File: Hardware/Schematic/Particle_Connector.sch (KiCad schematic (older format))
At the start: 10 parts, among them J1 Conn_01x12, J2 Conn_01x12, J6 Conn_01x12, J7 Conn_01x12

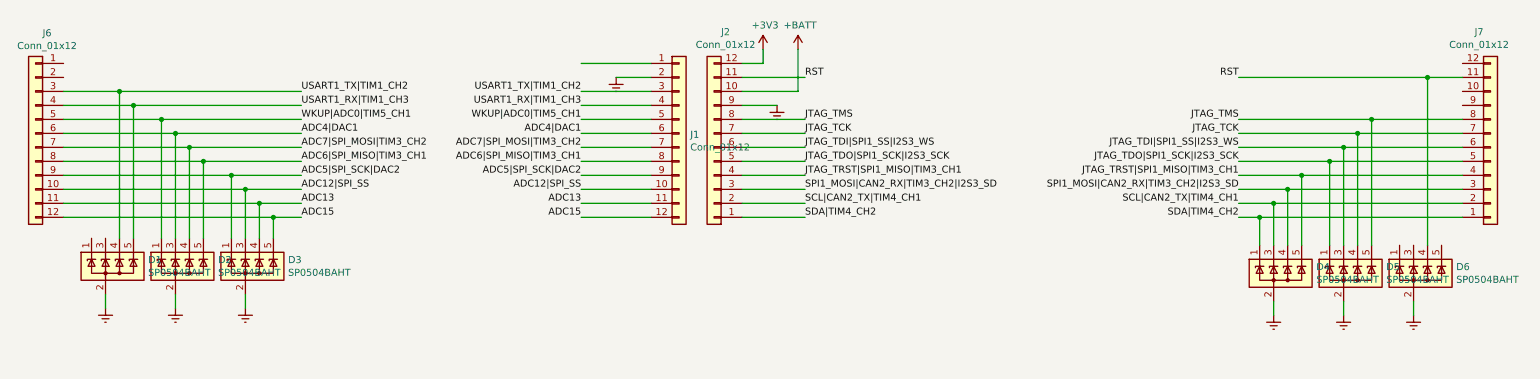
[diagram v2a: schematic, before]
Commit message: Lots of schematic updates
Lots of stuff...

* Added a new 8-pin TVS diode array
* Finalized the display connector
* Corrected the net labels to global labels so they span across sheets
* Added a 5V linear voltage regulator and LEDs to debug power
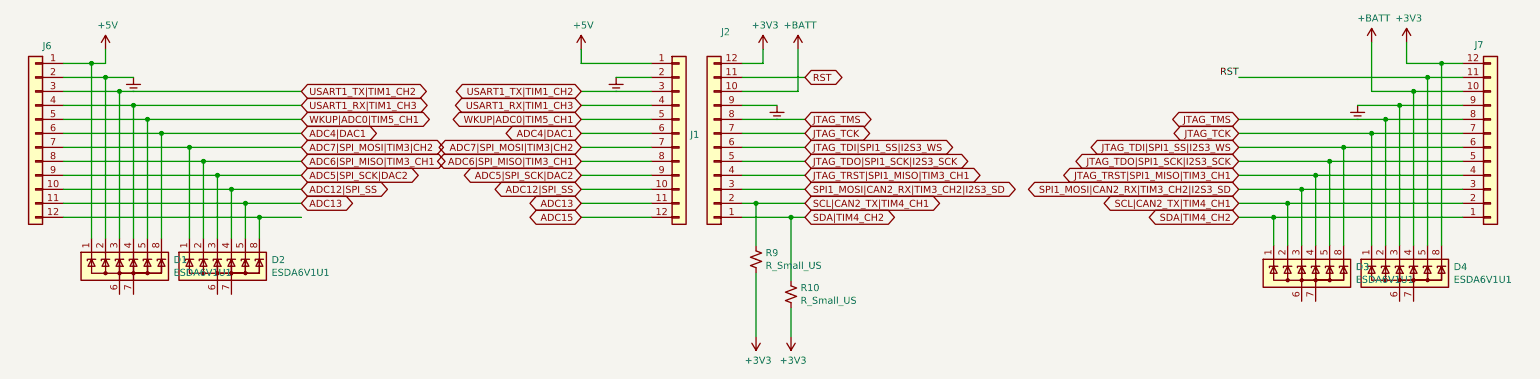
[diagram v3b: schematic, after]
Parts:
- removed D1, D2, D3, D4, D5, D6: SP0504BAHT, Package_TO_SOT_SMD:SOT-23-5, symbol Power_Protection:SP0504BAHT
- added D1, D2, D3, D4: ESDA6V1U1, ESDA6V1U1:SOIC127P600X175-8N, symbol Power_Protection:ESDA6V1U1
- added R10, R9: R_Small_US, Resistor_SMD:R_2512_6332Metric_Pad1.52x3.35mm_HandSolder, symbol Device:R_Small_US
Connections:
- net +3V3: now also J7.12 (Pin_12), D4.8 (K), R10.2, R9.2
- net +BATT: now also J7.10 (Pin_10), D4.4 (K)
- net ADC12|SPI_SS: now also D2.4 (K)
- net ADC13: now also D2.5 (K)
- net ADC15: no longer J6.12 (Pin_12)
- net ADC4|DAC1: now also D1.8 (K)
- net ADC5|SPI_SCK|DAC2: now also D2.3 (K)
- net ADC6|SPI_MISO|TIM3_CH1: now also D2.2 (K)
- net Earth: now also J6.2 (Pin_2), J7.9 (Pin_9), D1.2 (K), D4.3 (K)
- net JTAG_TCK: now also D4.1 (K)
- net JTAG_TDI|SPI1_SS|I2S3_WS: now also D3.8 (K)
- net JTAG_TDO|SPI1_SCK|I2S3_SCK: now also D3.5 (K)
- net JTAG_TMS: now also D4.2 (K)
- net JTAG_TRST|SPI1_MISO|TIM3_CH1: now also D3.4 (K)
- net RST: now also D4.5 (K)
- net SCL|CAN2_TX|TIM4_CH1: now also D3.2 (K), R9.1
- net SDA|TIM4_CH2: now also D3.1 (K), R10.1
- net SPI1_MOSI|CAN2_RX|TIM3_CH2|I2S3_SD: now also D3.3 (K)
- net USART1_RX|TIM1_CH3: now also D1.4 (K)
- net USART1_TX|TIM1_CH2: now also D1.3 (K)
- net WKUP|ADC0|TIM5_CH1: now also D1.5 (K)
- net +5V: now reaches J1.1 (Pin_1)
- net +5V: now also J6.1 (Pin_1), D1.1 (K)
- net ADC7|SPI_MOSI|TIM3_CH2 renamed ADC7|SPI_MOSI|TIM3|CH2
- net ADC7|SPI_MOSI|TIM3|CH2: now also D2.1 (K)
- new net: D2.8 (K), J6.12 (Pin_12)

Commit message: Added pogo-pin test points for "Extra" photon lines. Also added a 32-pin vertical header for connecting multiple smaller boards.
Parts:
- added J11, J12, J14, J15, J16, J17, J18: Conn_01x01, TestPoint:TestPoint_THTPad_1.0x1.0mm_Drill0.5mm, symbol Connector_Generic:Conn_01x01
- added J?: Conn_01x32, Connector_PinHeader_1.00mm:PinHeader_1x32_P1.00mm_Horizontal, symbol Connector_Generic:Conn_01x32
- D1, D2, D3, D4: symbol Power_Protection:ESDA6V1U1 -> WiFiLMR-rescue:ESDA6V1U1-Power_Protection
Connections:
- net +3V3: now also J?.24 (Pin_24)
- net +5V: now also J?.1 (Pin_1)
- net +BATT: now also J?.22 (Pin_22)
- net ADC12|SPI_SS: now also J?.10 (Pin_10)
- net ADC13: now also J?.11 (Pin_11)
- net ADC15: now also J?.12 (Pin_12)
- net ADC4|DAC1: now also J?.6 (Pin_6)
- net ADC5|SPI_SCK|DAC2: now also J?.9 (Pin_9)
- net ADC6|SPI_MISO|TIM3_CH1: now also J?.8 (Pin_8)
- net ADC7|SPI_MOSI|TIM3|CH2: now also J?.7 (Pin_7)
- net Earth: now also J?.2 (Pin_2), J?.21 (Pin_21), J?.32 (Pin_32)
- net JTAG_TCK: now also J?.19 (Pin_19)
- net JTAG_TDI|SPI1_SS|I2S3_WS: now also J?.18 (Pin_18)
- net JTAG_TDO|SPI1_SCK|I2S3_SCK: now also J?.17 (Pin_17)
- net JTAG_TMS: now also J?.20 (Pin_20)
- net JTAG_TRST|SPI1_MISO|TIM3_CH1: now also J?.16 (Pin_16)
- net RST: now also J?.23 (Pin_23)
- net SCL|CAN2_TX|TIM4_CH1: now also J?.14 (Pin_14)
- net SDA|TIM4_CH2: now also J?.13 (Pin_13)
- net SPI1_MOSI|CAN2_RX|TIM3_CH2|I2S3_SD: now also J?.15 (Pin_15)
- net USART1_RX|TIM1_CH3: now also J?.4 (Pin_4)
- net USART1_TX|TIM1_CH2: now also J?.3 (Pin_3)
- net WKUP|ADC0|TIM5_CH1: now also J?.5 (Pin_5)
- new net RGB_BLUE: J16.1 (Pin_1), J?.29 (Pin_29)
- new net RGB_GREEN: J12.1 (Pin_1), J?.28 (Pin_28)
- new net RGB_RED: J11.1 (Pin_1), J?.27 (Pin_27)
- new net SETUP_BUTTON: J15.1 (Pin_1), J?.26 (Pin_26)
- new net SMPS_ENABLE: J14.1 (Pin_1), J?.25 (Pin_25)
- new net USB_DATA+: J18.1 (Pin_1), J?.31 (Pin_31)
- new net USB_DATA-: J17.1 (Pin_1), J?.30 (Pin_30)

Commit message: Misc changes I forgot to commit.
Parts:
- gave numbers to parts that had none: 1
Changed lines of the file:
@@
 $EndComp
 $Comp
-L Connector_Generic:Conn_01x32 J?
+L Connector_Generic:Conn_01x32 J13
 U 1 1 5D101581
 P 3950 7100
-F 0 "J?" V 4075 7046 50  0000 C CNN
+F 0 "J13" V 4075 7046 50  0000 C CNN
 F 1 "Conn_01x32" V 4166 7046 50  0000 C CNN
 F 2 "Connector_PinHeader_1.00mm:PinHeader_1x32_P1.00mm_Horizontal" H 3950 7100 50  0001 C CNN
@@
 USART1_TX|TIM1_CH2
 $Comp
-L power:+5V #PWR?
+L power:+5V #PWR0109
 U 1 1 5D11DA94
 P 5450 6200
-F 0 "#PWR?" H 5450 6050 50  0001 C CNN
+F 0 "#PWR0109" H 5450 6050 50  0001 C CNN
 F 1 "+5V" H 5465 6373 50  0000 C CNN
 F 2 "" H 5450 6200 50  0001 C CNN
@@
 P 3350 6200
 AR Path="/5D141AB3" Ref="#PWR?"  Part="1"
-AR Path="/5D01AE82/5D141AB3" Ref="#PWR?"  Part="1"
-F 0 "#PWR?" H 3350 6050 50  0001 C CNN
+AR Path="/5D01AE82/5D141AB3" Ref="#PWR0110"  Part="1"
+F 0 "#PWR0110" H 3350 6050 50  0001 C CNN
 F 1 "+BATT" H 3365 6373 50  0000 C CNN
 F 2 "" H 3350 6200 50  0001 C CNN
@@
 P 3150 6200
 AR Path="/5D141A9E" Ref="#PWR?"  Part="1"
-AR Path="/5D01AE82/5D141A9E" Ref="#PWR?"  Part="1"
-F 0 "#PWR?" H 3150 6050 50  0001 C CNN
+AR Path="/5D01AE82/5D141A9E" Ref="#PWR0111"  Part="1"
+F 0 "#PWR0111" H 3150 6050 50  0001 C CNN
 F 1 "+3V3" H 3165 6373 50  0000 C CNN
 F 2 "" H 3150 6200 50  0001 C CNN
@@
 	2350 6750 2200 6750
 $Comp
-L power:Earth #PWR?
+L power:Earth #PWR0112
 U 1 1 5D1E44BC
 P 2200 6750
-F 0 "#PWR?" H 2200 6500 50  0001 C CNN
+F 0 "#PWR0112" H 2200 6500 50  0001 C CNN
 F 1 "Earth" H 2200 6600 50  0001 C CNN
 F 2 "" H 2200 6750 50  0001 C CNN
